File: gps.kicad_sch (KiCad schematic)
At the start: 10 parts, among them IC1 BGA824N6E6329XTSA1, J3 73412-0110, U10 MAX-M8Q

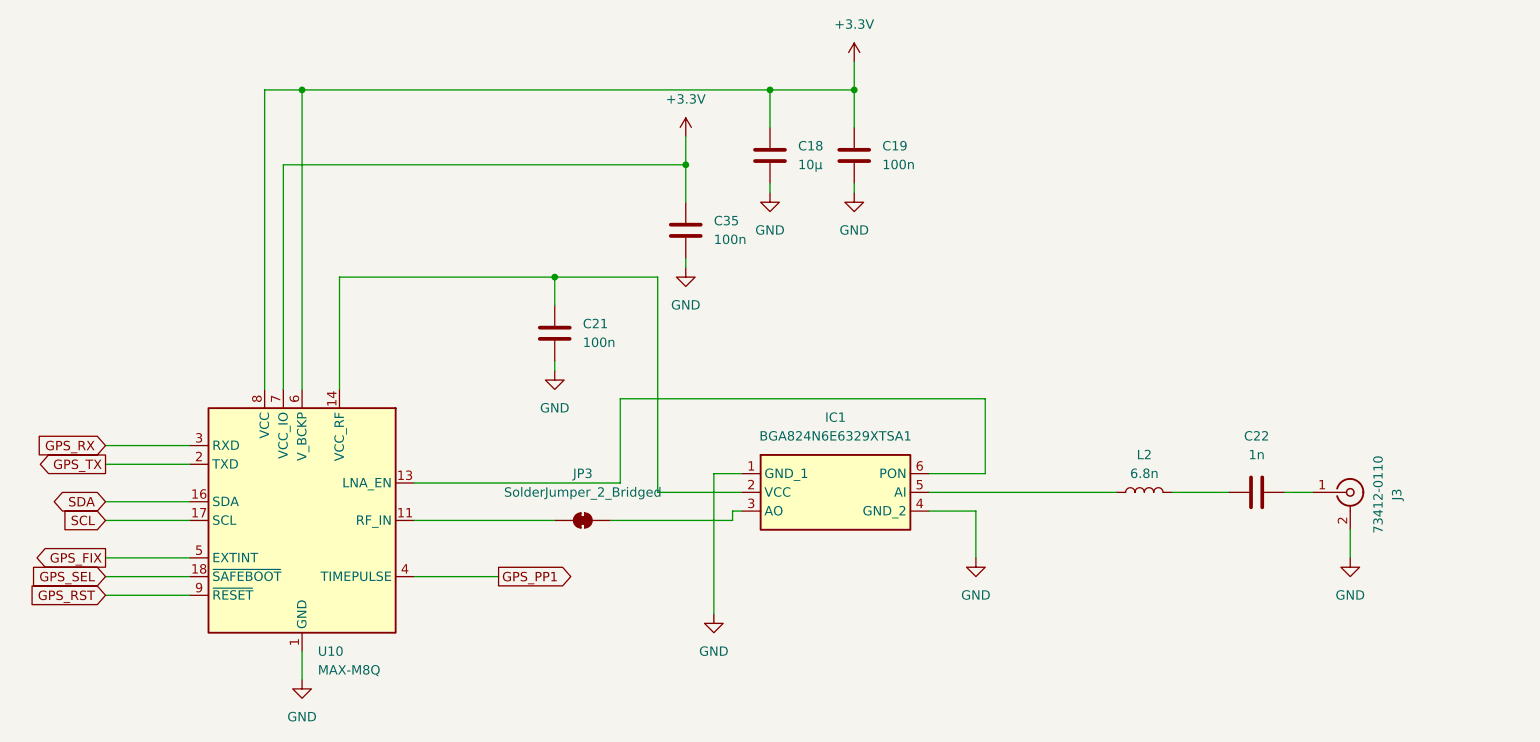
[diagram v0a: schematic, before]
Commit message: reduce board size
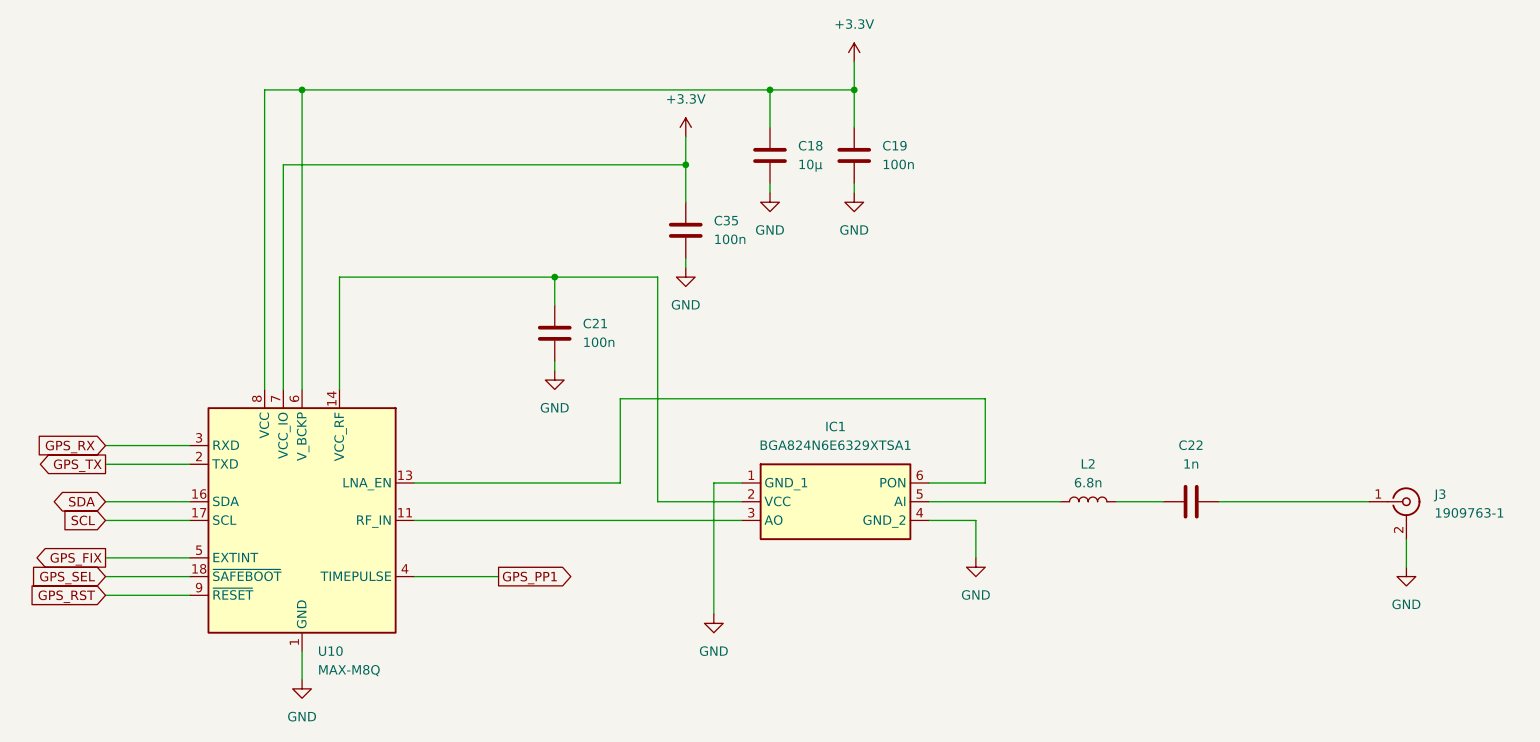
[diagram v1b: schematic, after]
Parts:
- removed JP3: SolderJumper_2_Bridged, Jumper:SolderJumper-2_P1.3mm_Bridged2Bar_RoundedPad1.0x1.5mm, symbol Jumper:SolderJumper_2_Bridged
- J3: value 73412-0110 -> 1909763-1; JLCPCB Part # C434806 -> 1909763-1; manf# 73412-0110 -> 1909763-1
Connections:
- net at U10.11 (RF_IN): now also IC1.3 (AO)
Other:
- moved on the sheet: C22, IC1, L2
